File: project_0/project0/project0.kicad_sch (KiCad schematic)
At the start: 3 parts

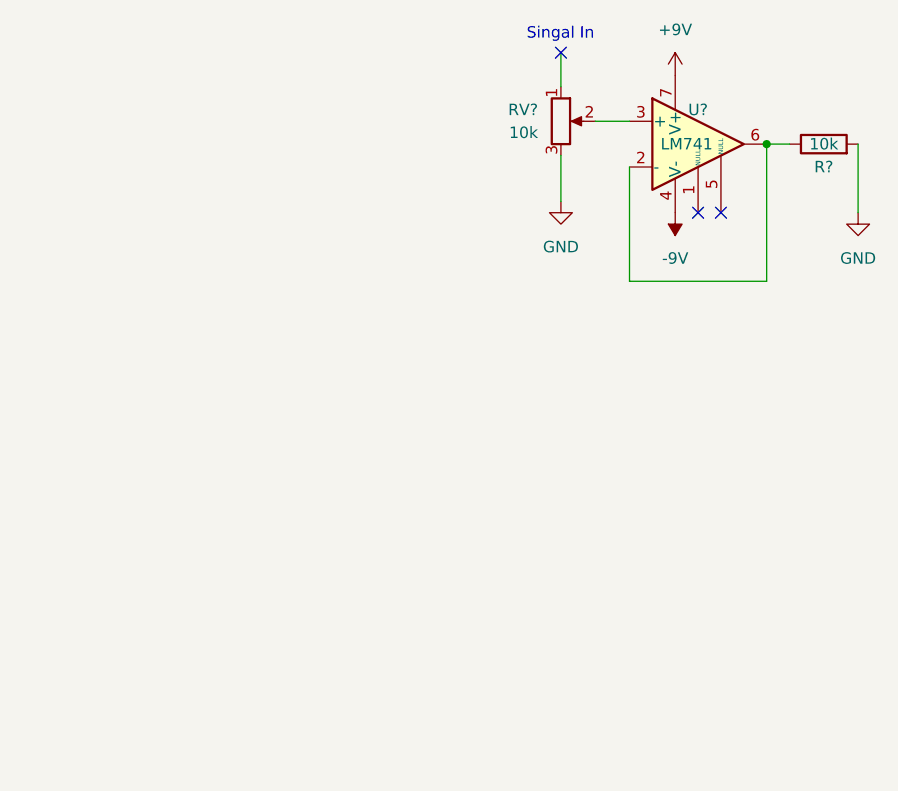
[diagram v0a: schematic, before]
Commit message: añado el archivo que ignora las librerias y actualizo la info de la tesis, están todos los circuitos ya hechos, al menos en esquemático, revisar footprints
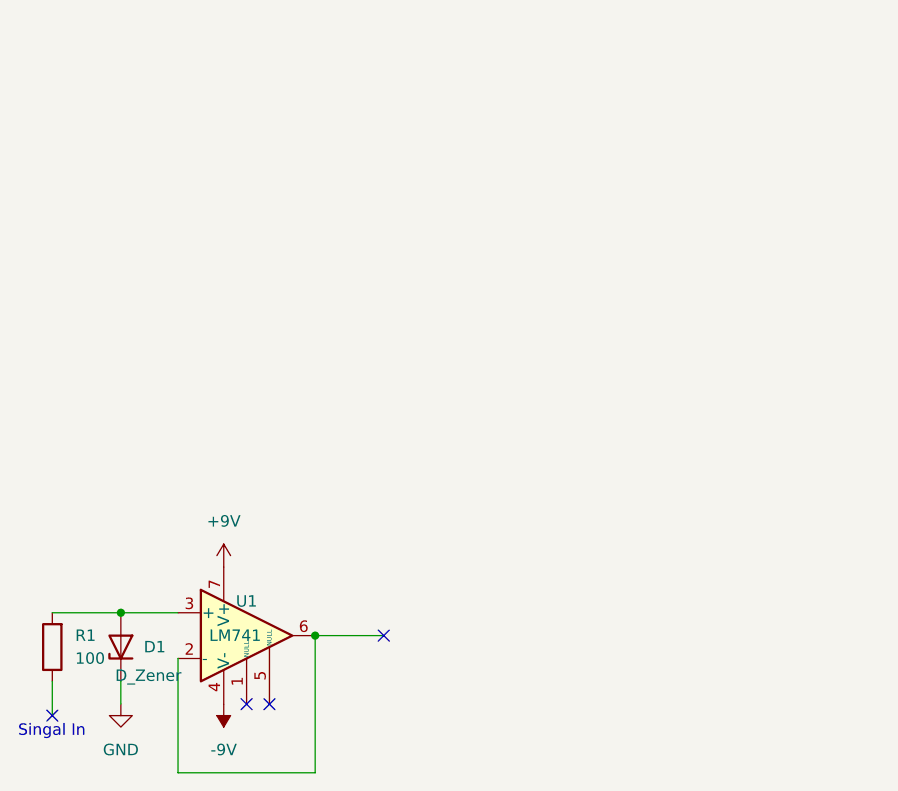
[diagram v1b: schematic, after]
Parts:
- removed R?: 10k, symbol Device:R
- removed RV?: 10k, symbol Device:R_Potentiometer
- added D1: D_Zener, Diode_THT:D_DO-201AE_P5.08mm_Vertical_KathodeUp, symbol Device:D_Zener
- added R1: 100, Resistor_THT:R_Axial_DIN0414_L11.9mm_D4.5mm_P7.62mm_Vertical, symbol Device:R
- U1: renamed from U?; footprint (none) -> LM741_THT:LM741-THT
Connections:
- net GND: now also D1.1 (K)
- net at U1.3 (+): now also D1.2 (A), R1.2
- no-connect marks 3 -> 4
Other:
- company: ThesisYT -> Yachay Tech - School of Physical Sciences and Nanotechnology
- title: 741_Buffer -> 741_Buffer_clipper
- moved on the sheet: U1
